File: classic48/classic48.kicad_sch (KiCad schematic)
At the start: 5 parts, among them SW1 Switch, U1 RP2040_Pro_Micro, U2 TRRS

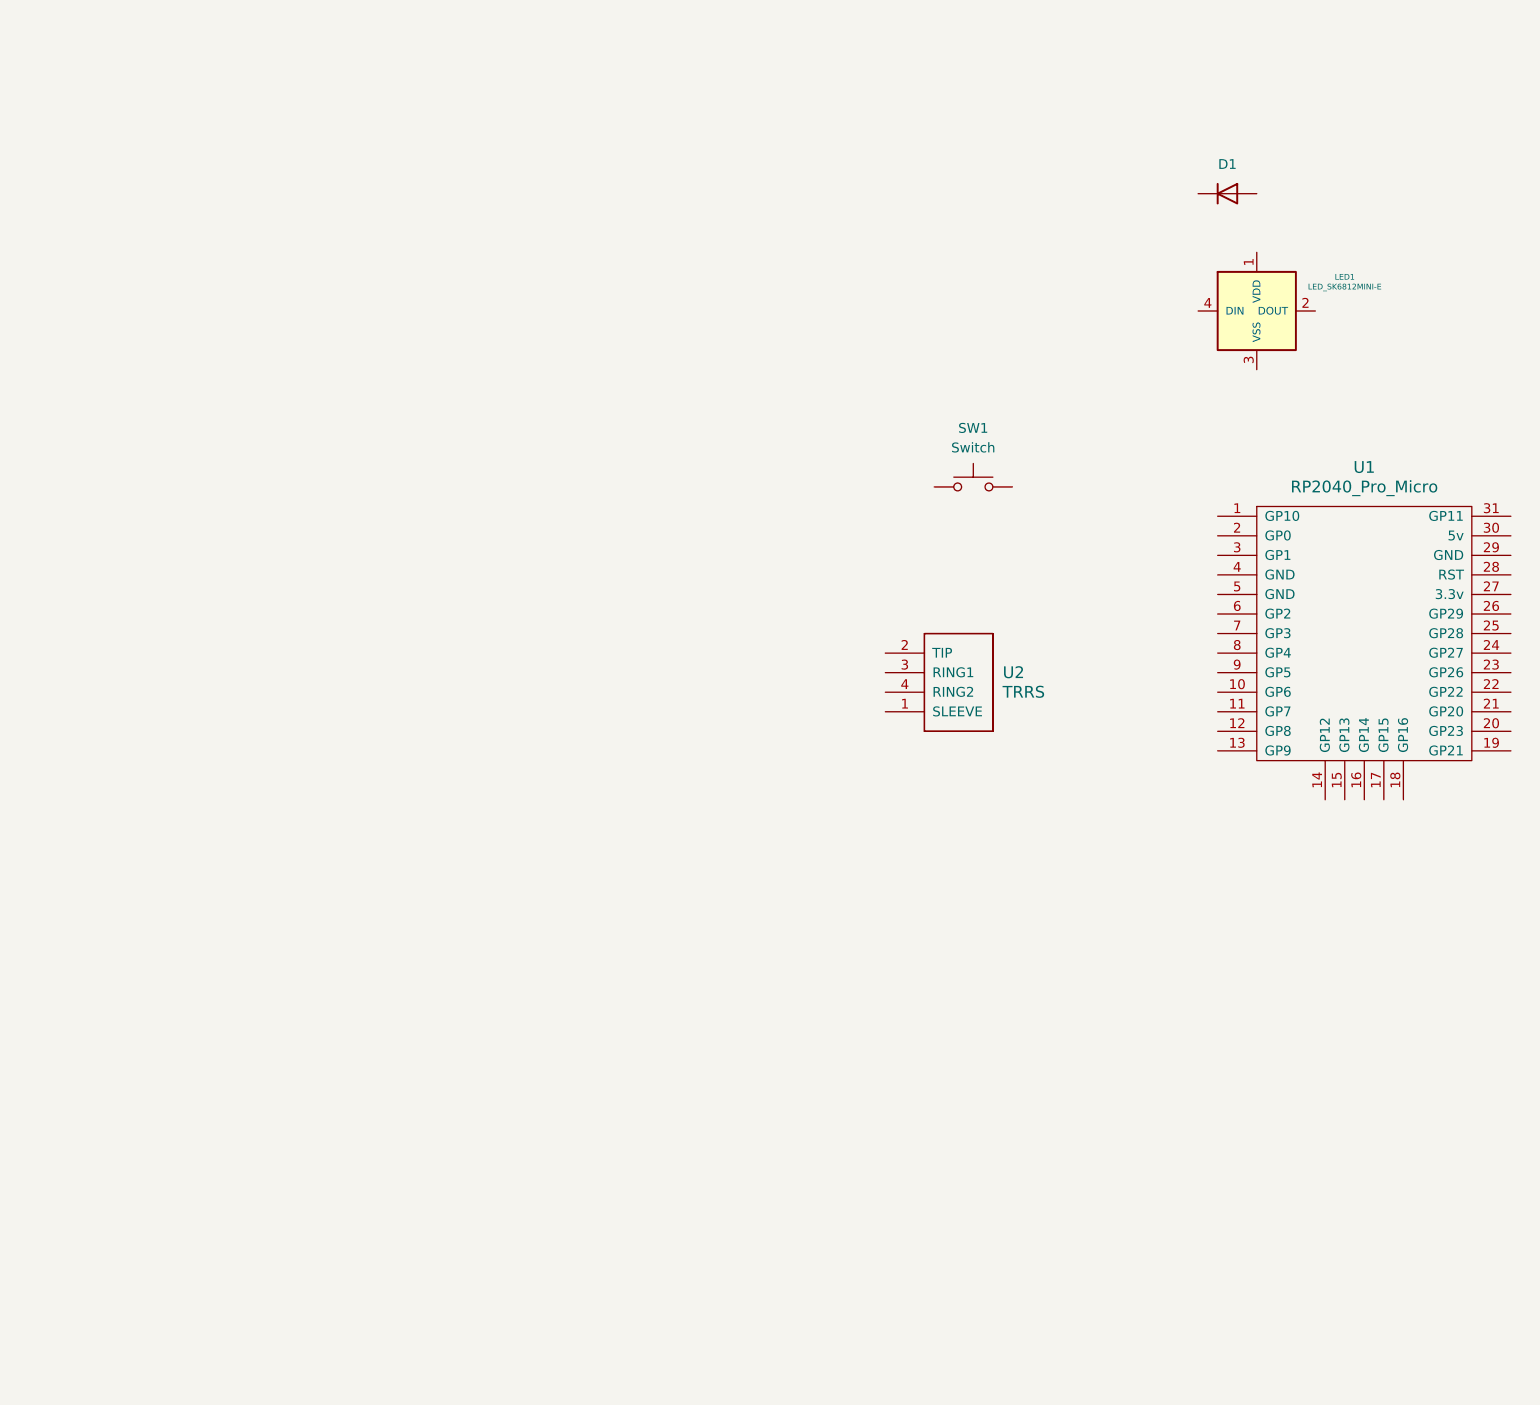
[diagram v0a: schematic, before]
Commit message: feat: schematic for left side
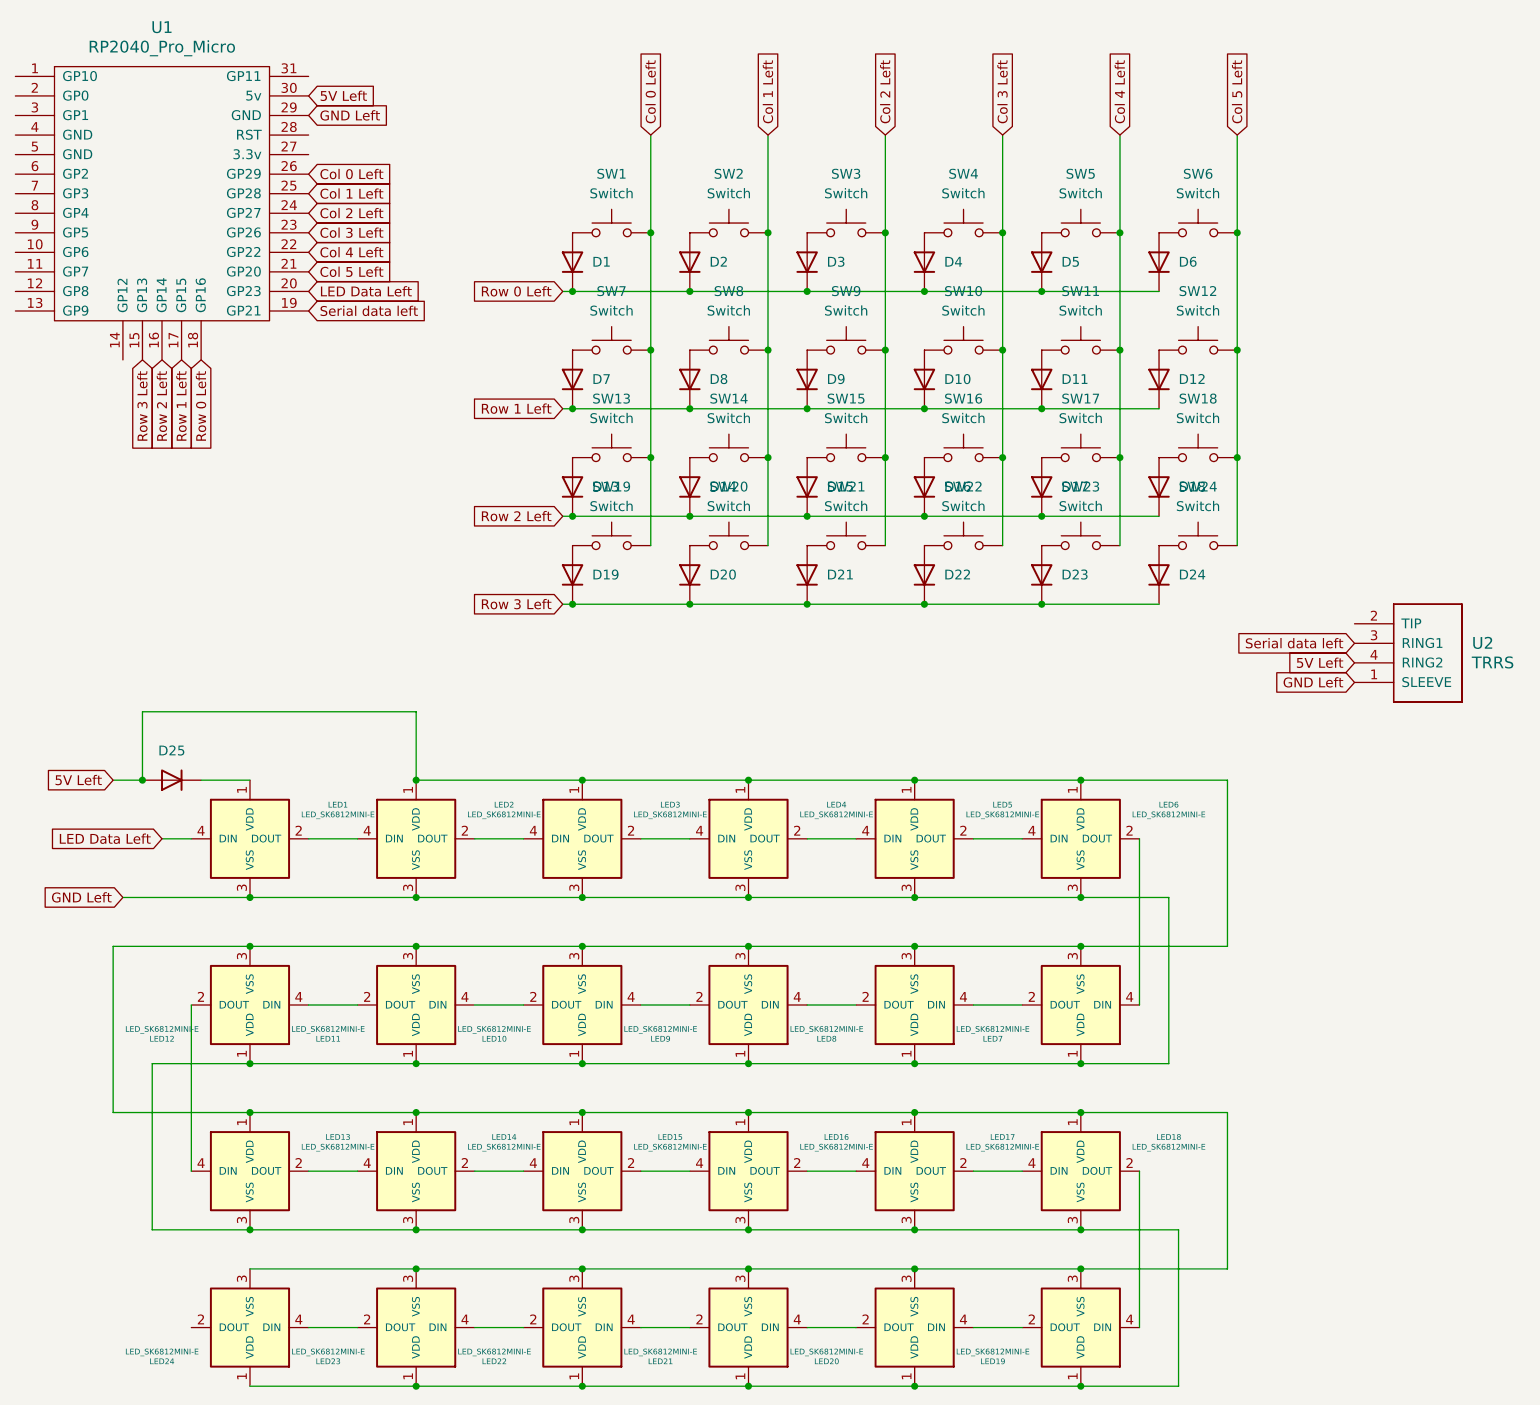
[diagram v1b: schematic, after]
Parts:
- added D10, D11, D12, D13, D14, D15, D16, D17, D18, D19, D2, D20, D21, D22, D23, D24, D25, D3, D4, D5, D6, D7, D8, D9: Diode_1N4148-SOD123, pjimenez:Diode_1N4148-SOD123, symbol pjimenez:Diode_1N4148-SOD123
- added LED10, LED11, LED12, LED13, LED14, LED15, LED16, LED17, LED18, LED19, LED2, LED20, LED21, LED22, LED23, LED24, LED3, LED4, LED5, LED6, LED7, LED8, LED9: LED_SK6812MINI-E, pjimenez:LED_SK6812-MINI-E, symbol pjimenez:LED_SK6812MINI-E
- added SW10, SW11, SW12, SW13, SW14, SW15, SW16, SW17, SW18, SW19, SW2, SW20, SW21, SW22, SW23, SW24, SW3, SW4, SW5, SW6, SW7, SW8, SW9: Switch, pjimenez:Switch_ChocV1-hotswap, symbol pjimenez:Switch_ChocV1-hotswap
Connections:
- net Row 0 Left: now reaches D1.1 (K)
- net Row 0 Left: now also U1.18 (GP16), D2.1 (K), D3.1 (K), D4.1 (K), D5.1 (K), D6.1 (K)
- net at D1.2 (A): now also SW1.1
- net Col 0 Left: now reaches SW1.2
- net Col 0 Left: now also U1.26 (GP29), SW13.2, SW19.2, SW7.2
- net GND Left: now reaches U2.1 (SLEEVE)
- net GND Left: now also LED1.3 (VSS), U1.29 (GND), LED10.1 (VDD), LED11.1 (VDD), LED12.1 (VDD), LED13.3 (VSS), LED14.3 (VSS), LED15.3 (VSS), LED16.3 (VSS), LED17.3 (VSS), LED18.3 (VSS), LED19.1 (VDD), LED2.3 (VSS), LED20.1 (VDD), LED21.1 (VDD), LED22.1 (VDD), LED23.1 (VDD), LED24.1 (VDD), LED3.3 (VSS), LED4.3 (VSS), LED5.3 (VSS), LED6.3 (VSS), LED7.1 (VDD), LED8.1 (VDD), LED9.1 (VDD)
- net Serial data left: now reaches U2.3 (RING1)
- net Serial data left: now also U1.19 (GP21)
- net 5V Left: now reaches U2.4 (RING2)
- net 5V Left: now also U1.30 (5v), D25.2 (A), LED10.3 (VSS), LED11.3 (VSS), LED12.3 (VSS), LED13.1 (VDD), LED14.1 (VDD), LED15.1 (VDD), LED16.1 (VDD), LED17.1 (VDD), LED18.1 (VDD), LED19.3 (VSS), LED2.1 (VDD), LED20.3 (VSS), LED21.3 (VSS), LED22.3 (VSS), LED23.3 (VSS), LED24.3 (VSS), LED3.1 (VDD), LED4.1 (VDD), LED5.1 (VDD), LED6.1 (VDD), LED7.3 (VSS), LED8.3 (VSS), LED9.3 (VSS)
- net at LED1.1 (VDD): now also D25.1 (K)
- net at LED1.2 (DOUT): now also LED2.4 (DIN)
- net LED Data Left: now reaches LED1.4 (DIN)
- net LED Data Left: now also U1.20 (GP23)
- net Row 3 Left: now reaches U1.15 (GP13)
- net Row 3 Left: now also D19.1 (K), D20.1 (K), D21.1 (K), D22.1 (K), D23.1 (K), D24.1 (K)
- net Row 2 Left: now reaches U1.16 (GP14)
- net Row 2 Left: now also D13.1 (K), D14.1 (K), D15.1 (K), D16.1 (K), D17.1 (K), D18.1 (K)
- net Row 1 Left: now reaches U1.17 (GP15)
- net Row 1 Left: now also D10.1 (K), D11.1 (K), D12.1 (K), D7.1 (K), D8.1 (K), D9.1 (K)
- net Col 5 Left: now reaches U1.21 (GP20)
- net Col 5 Left: now also SW12.2, SW18.2, SW24.2, SW6.2
- net Col 4 Left: now reaches U1.22 (GP22)
- net Col 4 Left: now also SW11.2, SW17.2, SW23.2, SW5.2
- net Col 3 Left: now reaches U1.23 (GP26)
- net Col 3 Left: now also SW10.2, SW16.2, SW22.2, SW4.2
- net Col 2 Left: now reaches U1.24 (GP27)
- net Col 2 Left: now also SW15.2, SW21.2, SW3.2, SW9.2
- net Col 1 Left: now reaches U1.25 (GP28)
- net Col 1 Left: now also SW14.2, SW2.2, SW20.2, SW8.2
- new net: D8.2 (A), SW8.1
- new net: LED8.2 (DOUT), LED9.4 (DIN)
- new net: LED7.2 (DOUT), LED8.4 (DIN)
- new net: D6.2 (A), SW6.1
- new net: D15.2 (A), SW15.1
- new net: D4.2 (A), SW4.1
- new net: LED16.2 (DOUT), LED17.4 (DIN)
- new net: LED15.2 (DOUT), LED16.4 (DIN)
- new net: D14.2 (A), SW14.1
- new net: LED2.2 (DOUT), LED3.4 (DIN)
- new net: D9.2 (A), SW9.1
- new net: D16.2 (A), SW16.1
- new net: LED12.2 (DOUT), LED13.4 (DIN)
- new net: LED11.2 (DOUT), LED12.4 (DIN)
- new net: LED21.2 (DOUT), LED22.4 (DIN)
- new net: LED20.2 (DOUT), LED21.4 (DIN)
- new net: D5.2 (A), SW5.1
- new net: LED4.2 (DOUT), LED5.4 (DIN)
- new net: LED3.2 (DOUT), LED4.4 (DIN)
- new net: D24.2 (A), SW24.1
- new net: LED5.2 (DOUT), LED6.4 (DIN)
- new net: LED23.2 (DOUT), LED24.4 (DIN)
- new net: LED10.2 (DOUT), LED11.4 (DIN)
- new net: LED10.4 (DIN), LED9.2 (DOUT)
- new net: D3.2 (A), SW3.1
- new net: LED22.2 (DOUT), LED23.4 (DIN)
- new net: D22.2 (A), SW22.1
- new net: D2.2 (A), SW2.1
- new net: LED18.2 (DOUT), LED19.4 (DIN)
- new net: LED17.2 (DOUT), LED18.4 (DIN)
- new net: D21.2 (A), SW21.1
- new net: D23.2 (A), SW23.1
- new net: LED13.2 (DOUT), LED14.4 (DIN)
- new net: LED6.2 (DOUT), LED7.4 (DIN)
- new net: D13.2 (A), SW13.1
- new net: LED14.2 (DOUT), LED15.4 (DIN)
- new net: LED19.2 (DOUT), LED20.4 (DIN)
- new net: D10.2 (A), SW10.1
- new net: D18.2 (A), SW18.1
- new net: D20.2 (A), SW20.1
- new net: D17.2 (A), SW17.1
- new net: D11.2 (A), SW11.1
- new net: D19.2 (A), SW19.1
- new net: D12.2 (A), SW12.1
- new net: D7.2 (A), SW7.1
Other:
- moved on the sheet: LED1, SW1, U1, U2

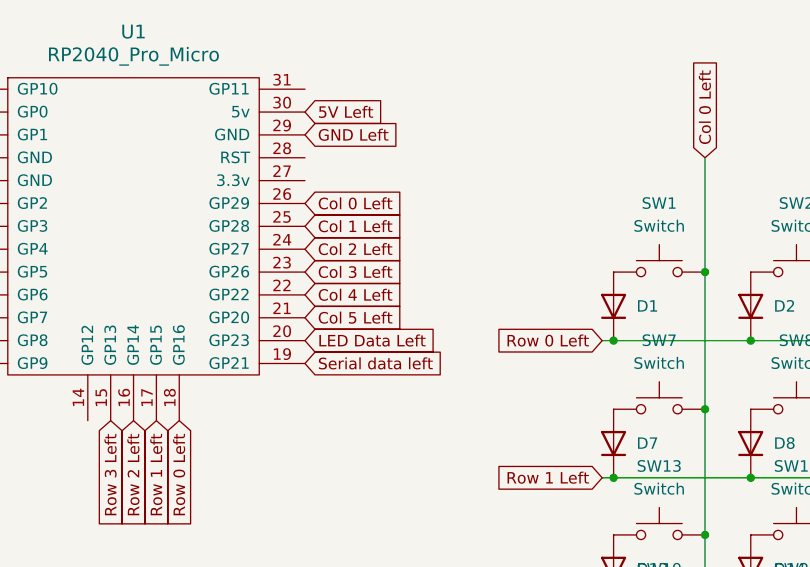
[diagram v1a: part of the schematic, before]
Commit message: feat: LEDs and TRRS fully connected
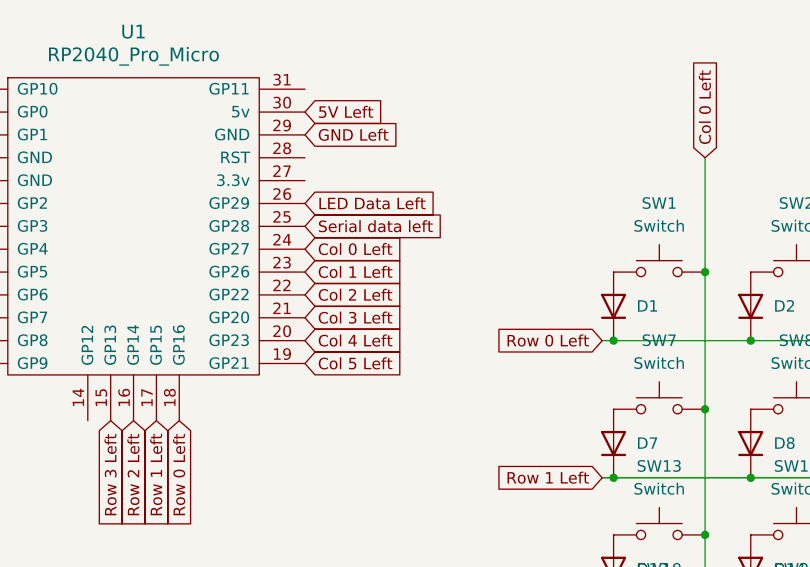
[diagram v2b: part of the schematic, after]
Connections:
- net Col 0 Left: now also U1.24 (GP27); no longer U1.26 (GP29)
- net Col 1 Left: now also U1.23 (GP26); no longer U1.25 (GP28)
- net Col 2 Left: now also U1.22 (GP22); no longer U1.24 (GP27)
- net Col 3 Left: now also U1.21 (GP20); no longer U1.23 (GP26)
- net Col 4 Left: now also U1.20 (GP23); no longer U1.22 (GP22)
- net Col 5 Left: now also U1.19 (GP21); no longer U1.21 (GP20)
- net LED Data Left: now also U1.26 (GP29); no longer U1.20 (GP23)
- net Serial data left: now also U1.25 (GP28); no longer U1.19 (GP21)

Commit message: feat: finish tracks
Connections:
- net Col 0 Left: now also U1.20 (GP23); no longer U1.24 (GP27)
- net Col 1 Left: now also U1.19 (GP21); no longer U1.23 (GP26)
- net Col 2 Left: now also U1.18 (GP16); no longer U1.22 (GP22)
- net Col 3 Left: now also U1.17 (GP15); no longer U1.21 (GP20)
- net Col 4 Left: now also U1.16 (GP14); no longer U1.20 (GP23)
- net Col 5 Left: now also U1.15 (GP13); no longer U1.19 (GP21)
- net Row 0 Left: now also U1.24 (GP27); no longer U1.18 (GP16)
- net Row 1 Left: now also U1.23 (GP26); no longer U1.17 (GP15)
- net Row 2 Left: now also U1.22 (GP22); no longer U1.16 (GP14)
- net Row 3 Left: now also U1.21 (GP20); no longer U1.15 (GP13)

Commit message: fix: left side LEDs were connected incorrectly feat: right side schema
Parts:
- added D26, D27, D28, D29, D30, D31, D32, D33, D34, D35, D36, D37, D38, D39, D40, D41, D42, D43, D44, D45, D46, D47, D48, D49, D50: Diode_1N4148-SOD123, pjimenez:Diode_1N4148-SOD123, symbol pjimenez:Diode_1N4148-SOD123
- added LED25, LED26, LED27, LED28, LED29, LED30, LED31, LED32, LED33, LED34, LED35, LED36, LED37, LED38, LED39, LED40, LED41, LED42, LED43, LED44, LED45, LED46, LED47, LED48: LED_SK6812MINI-E, pjimenez:LED_SK6812-MINI-E, symbol pjimenez:LED_SK6812MINI-E
- added SW25, SW26, SW27, SW28, SW29, SW30, SW31, SW32, SW33, SW34, SW35, SW36, SW37, SW38, SW39, SW40, SW41, SW42, SW43, SW44, SW45, SW46, SW47, SW48: Switch, pjimenez:Switch_ChocV1-hotswap, symbol pjimenez:Switch_ChocV1-hotswap
- added U3: RP2040_Pro_Micro, pjimenez:RP2040_Pro_Micro, symbol pjimenez:MCU_RP2040_Pro_Micro
- added U4: TRRS, pjimenez:TRRS_PJ-320A, symbol pjimenez:TRRS_PJ-320A
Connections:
- net 5V Left: now also LED10.1 (VDD), LED11.1 (VDD), LED12.1 (VDD), LED19.1 (VDD), LED20.1 (VDD), LED21.1 (VDD), LED22.1 (VDD), LED23.1 (VDD), LED24.1 (VDD), LED7.1 (VDD), LED8.1 (VDD), LED9.1 (VDD); no longer LED10.3 (VSS), LED11.3 (VSS), LED12.3 (VSS), LED19.3 (VSS), LED20.3 (VSS), LED21.3 (VSS), LED22.3 (VSS), LED23.3 (VSS), LED24.3 (VSS), LED7.3 (VSS), LED8.3 (VSS), LED9.3 (VSS)
- net GND Left: now also LED10.3 (VSS), LED11.3 (VSS), LED12.3 (VSS), LED19.3 (VSS), LED20.3 (VSS), LED21.3 (VSS), LED22.3 (VSS), LED23.3 (VSS), LED24.3 (VSS), LED7.3 (VSS), LED8.3 (VSS), LED9.3 (VSS); no longer LED10.1 (VDD), LED11.1 (VDD), LED12.1 (VDD), LED19.1 (VDD), LED20.1 (VDD), LED21.1 (VDD), LED22.1 (VDD), LED23.1 (VDD), LED24.1 (VDD), LED7.1 (VDD), LED8.1 (VDD), LED9.1 (VDD)
- net Serial data left renamed Serial data Left
- new net: LED47.2 (DOUT), LED48.4 (DIN)
- new net: LED37.2 (DOUT), LED38.4 (DIN)
- new net: LED36.2 (DOUT), LED37.4 (DIN)
- new net: D29.2 (A), SW28.1
- new net: LED43.2 (DOUT), LED44.4 (DIN)
- new net: LED42.2 (DOUT), LED43.4 (DIN)
- new net: D45.2 (A), SW44.1
- new net: LED41.2 (DOUT), LED42.4 (DIN)
- new net: LED40.2 (DOUT), LED41.4 (DIN)
- new net: D37.2 (A), SW36.1
- new net: D46.2 (A), SW45.1
- new net: LED35.2 (DOUT), LED36.4 (DIN)
- new net: D28.2 (A), SW27.1
- new net: D41.2 (A), SW40.1
- new net: D38.2 (A), SW37.1
- new net: LED34.2 (DOUT), LED35.4 (DIN)
- new net: LED33.2 (DOUT), LED34.4 (DIN)
- new net: D34.2 (A), SW33.1
- new net: D27.2 (A), SW26.1
- new net: LED27.2 (DOUT), LED28.4 (DIN)
- new net: LED26.2 (DOUT), LED27.4 (DIN)
- new net: LED29.2 (DOUT), LED30.4 (DIN)
- new net: LED28.2 (DOUT), LED29.4 (DIN)
- new net: LED31.2 (DOUT), LED32.4 (DIN)
- new net: LED30.2 (DOUT), LED31.4 (DIN)
- new net: D44.2 (A), SW43.1
- new net: D40.2 (A), SW39.1
- new net: D30.2 (A), SW29.1
- new net: D49.2 (A), SW48.1
- new net: D42.2 (A), SW41.1
- new net: LED39.2 (DOUT), LED40.4 (DIN)
- new net: D32.2 (A), SW31.1
- new net: D43.2 (A), SW42.1
- new net: D33.2 (A), SW32.1
- new net: D47.2 (A), SW46.1
- new net: LED38.2 (DOUT), LED39.4 (DIN)
- new net: D50.1 (K), LED25.1 (VDD)
- new net: LED25.2 (DOUT), LED26.4 (DIN)
- new net: D36.2 (A), SW35.1
- new net: D31.2 (A), SW30.1
- new net: LED32.2 (DOUT), LED33.4 (DIN)
- new net: D35.2 (A), SW34.1
- new net: D48.2 (A), SW47.1
- new net: D39.2 (A), SW38.1
- new net: LED44.2 (DOUT), LED45.4 (DIN)
- new net: LED46.2 (DOUT), LED47.4 (DIN)
- new net: LED45.2 (DOUT), LED46.4 (DIN)
- new net: D26.2 (A), SW25.1
- new net 5V Right: D50.2 (A), LED26.1 (VDD), LED27.1 (VDD), LED28.1 (VDD), LED29.1 (VDD), LED30.1 (VDD), LED31.1 (VDD), LED32.1 (VDD), LED33.1 (VDD), LED34.1 (VDD), LED35.1 (VDD), LED36.1 (VDD), LED37.1 (VDD), LED38.1 (VDD), LED39.1 (VDD), LED40.1 (VDD), LED41.1 (VDD), LED42.1 (VDD), LED43.1 (VDD), LED44.1 (VDD), LED45.1 (VDD), LED46.1 (VDD), LED47.1 (VDD), LED48.1 (VDD), U3.30 (5v), U4.4 (RING2)
- new net Col 0 Right: SW30.2, SW36.2, SW42.2, SW48.2, U3.20 (GP23)
- new net Col 1 Right: SW29.2, SW35.2, SW41.2, SW47.2, U3.19 (GP21)
- new net Col 2 Right: SW28.2, SW34.2, SW40.2, SW46.2, U3.18 (GP16)
- new net Col 3 Right: SW27.2, SW33.2, SW39.2, SW45.2, U3.17 (GP15)
- new net Col 4 Right: SW26.2, SW32.2, SW38.2, SW44.2, U3.16 (GP14)
- new net Col 5 Right: SW25.2, SW31.2, SW37.2, SW43.2, U3.15 (GP13)
- new net GND Right: LED25.3 (VSS), LED26.3 (VSS), LED27.3 (VSS), LED28.3 (VSS), LED29.3 (VSS), LED30.3 (VSS), LED31.3 (VSS), LED32.3 (VSS), LED33.3 (VSS), LED34.3 (VSS), LED35.3 (VSS), LED36.3 (VSS), LED37.3 (VSS), LED38.3 (VSS), LED39.3 (VSS), LED40.3 (VSS), LED41.3 (VSS), LED42.3 (VSS), LED43.3 (VSS), LED44.3 (VSS), LED45.3 (VSS), LED46.3 (VSS), LED47.3 (VSS), LED48.3 (VSS), U3.29 (GND), U4.1 (SLEEVE)
- new net LED data Right: LED25.4 (DIN), U3.26 (GP29)
- new net Row 0 Right: D26.1 (K), D27.1 (K), D28.1 (K), D29.1 (K), D30.1 (K), D31.1 (K), U3.24 (GP27)
- new net Row 1 Right: D32.1 (K), D33.1 (K), D34.1 (K), D35.1 (K), D36.1 (K), D37.1 (K), U3.23 (GP26)
- new net Row 2 Right: D38.1 (K), D39.1 (K), D40.1 (K), D41.1 (K), D42.1 (K), D43.1 (K), U3.22 (GP22)
- new net Row 3 Right: D44.1 (K), D45.1 (K), D46.1 (K), D47.1 (K), D48.1 (K), D49.1 (K), U3.21 (GP20)
- new net Serial data Right: U3.25 (GP28), U4.3 (RING1)
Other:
- moved on the sheet: U2
